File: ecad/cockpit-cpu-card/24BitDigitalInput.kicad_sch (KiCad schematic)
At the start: 79 parts, among them J10 Digital In, U10 74HC165, U11 74HC165, U9 74HC165

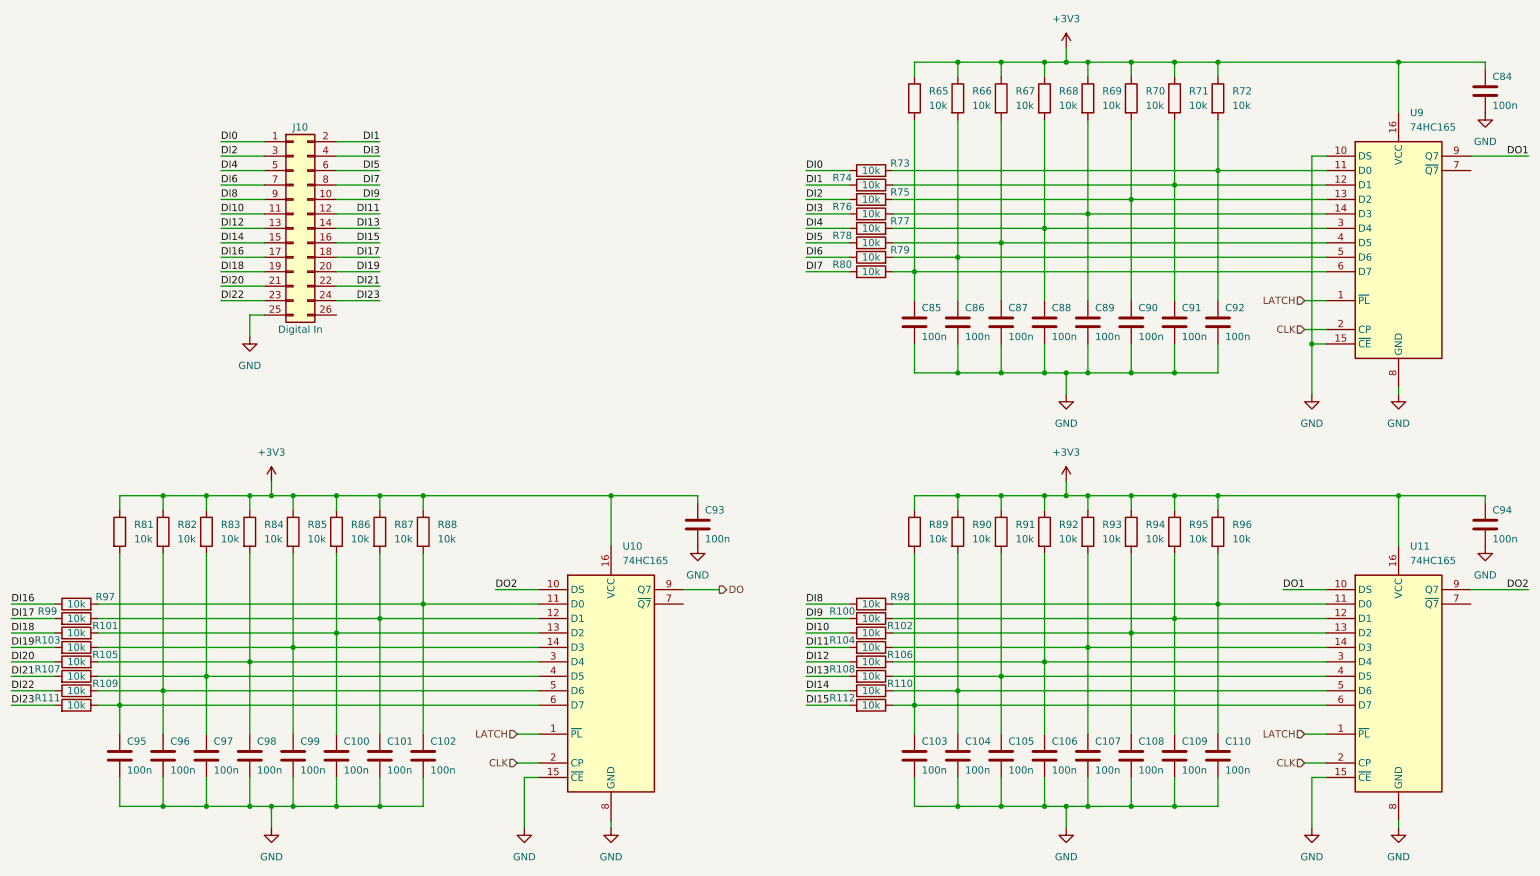
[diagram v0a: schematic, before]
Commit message: Fixing wrong resistor values
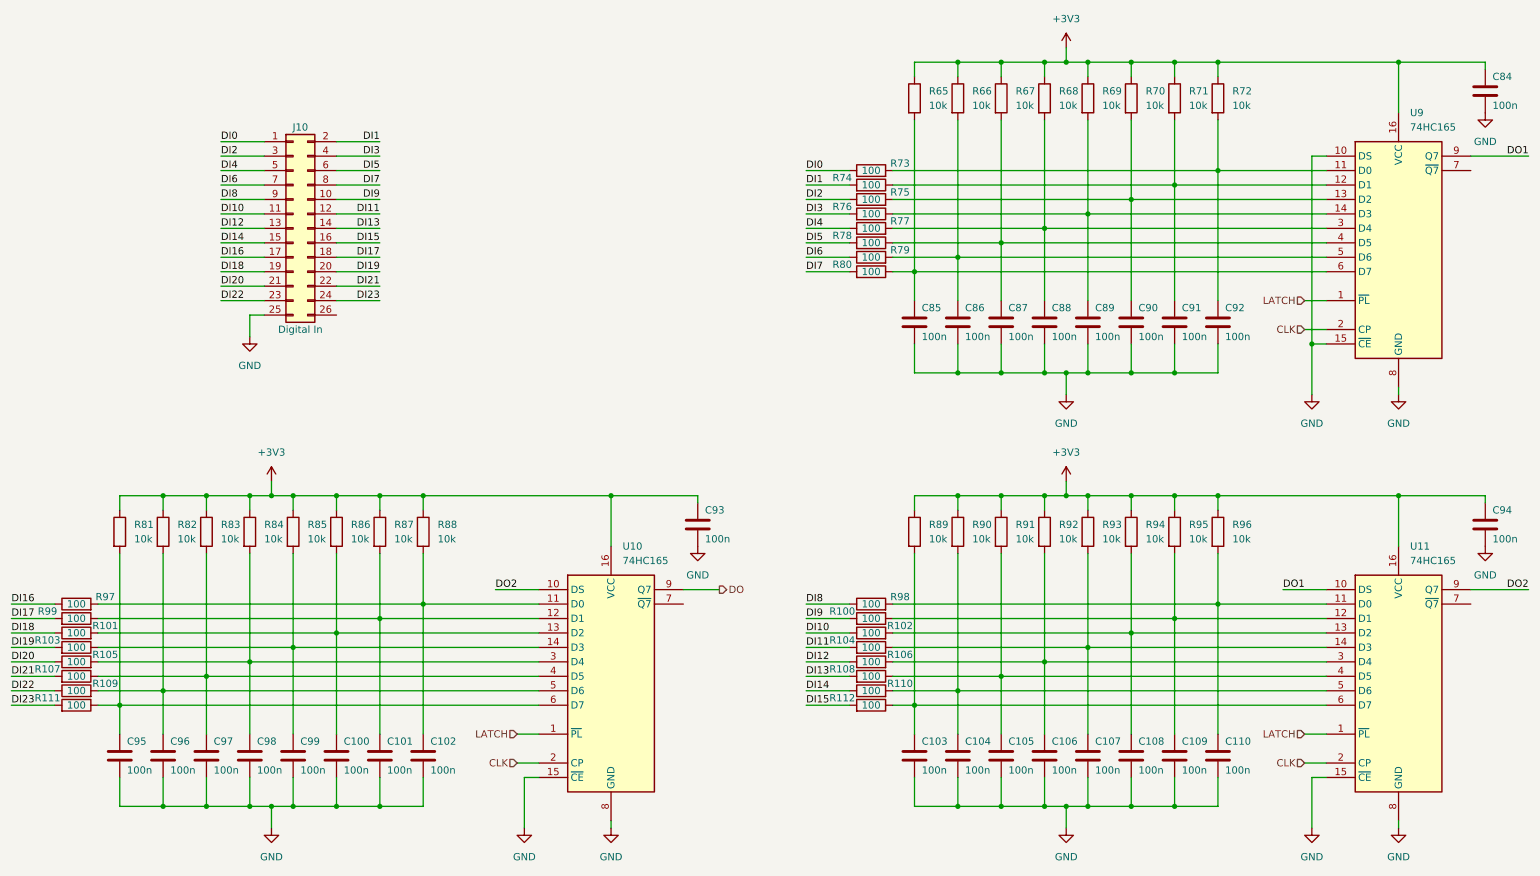
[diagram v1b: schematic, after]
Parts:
- R100, R101, R102, R103, R104, R105, R106, R107, R108, R109, R110, R111, R112, R73, R74, R75, R76, R77, R78, R79, R80, R97, R98, R99: value 10k -> 100; MPN MCMR06X103 JTL -> MCMR06X1000FTL; ON_FARNELL 2073356 -> 2073347

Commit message: 120R from Distrelec
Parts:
- R100, R101, R102, R103, R104, R105, R106, R107, R108, R109, R110, R111, R112, R73, R74, R75, R76, R77, R78, R79, R80, R97, R98, R99: value 100 -> 120; MPN MCMR06X1000FTL -> 1550603SAF1200T5E; ON_DISTRELEC (none) -> 300-56-474; ON_FARNELL 2073347 -> (none)
